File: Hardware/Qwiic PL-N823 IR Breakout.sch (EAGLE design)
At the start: 22 parts, among them U1 ADS1015, U2 LMV358, U3 PL-N823-01

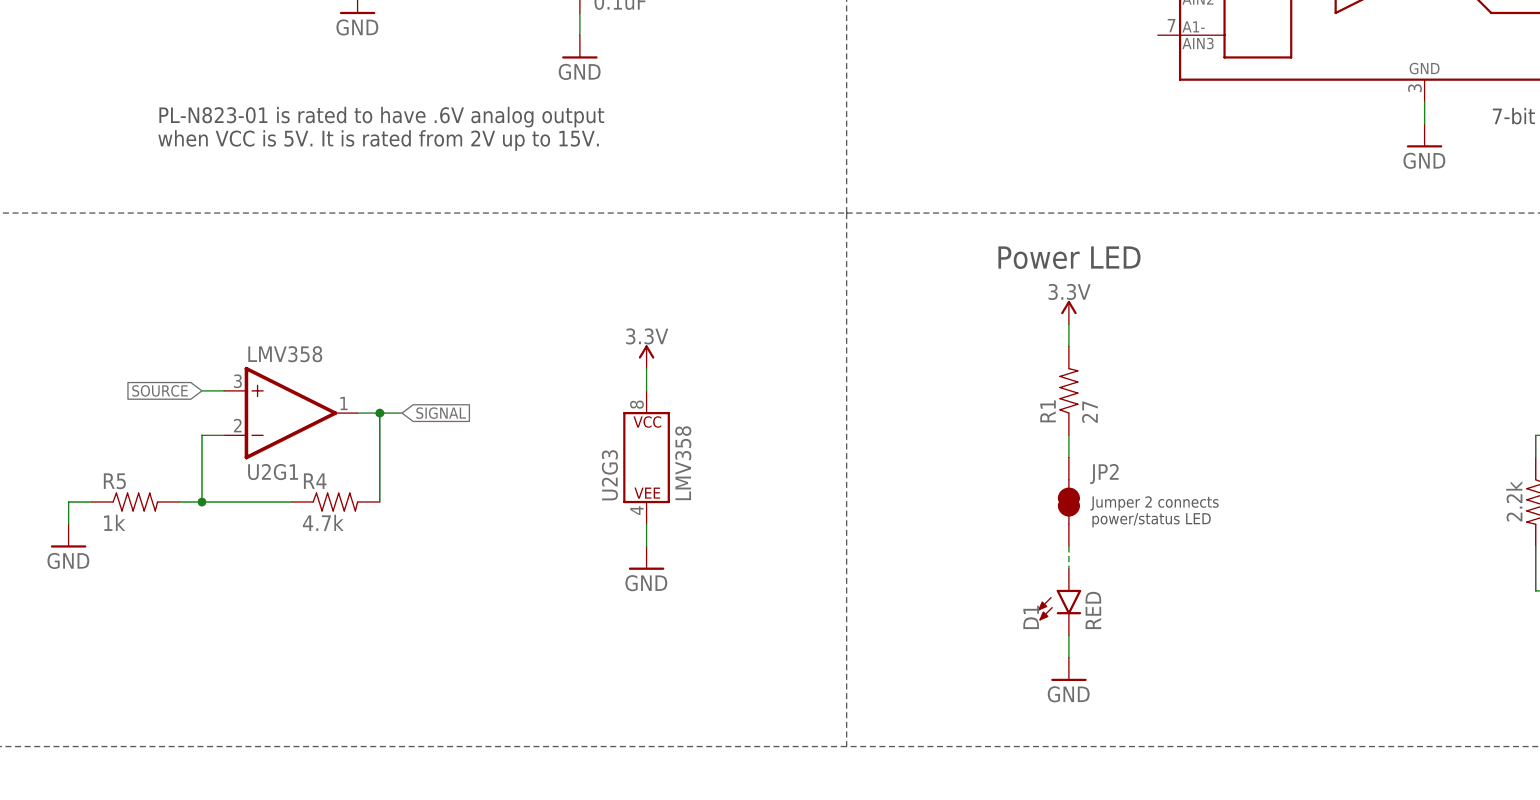
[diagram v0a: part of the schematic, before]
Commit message: Add no clean note. Change to blue power LED.
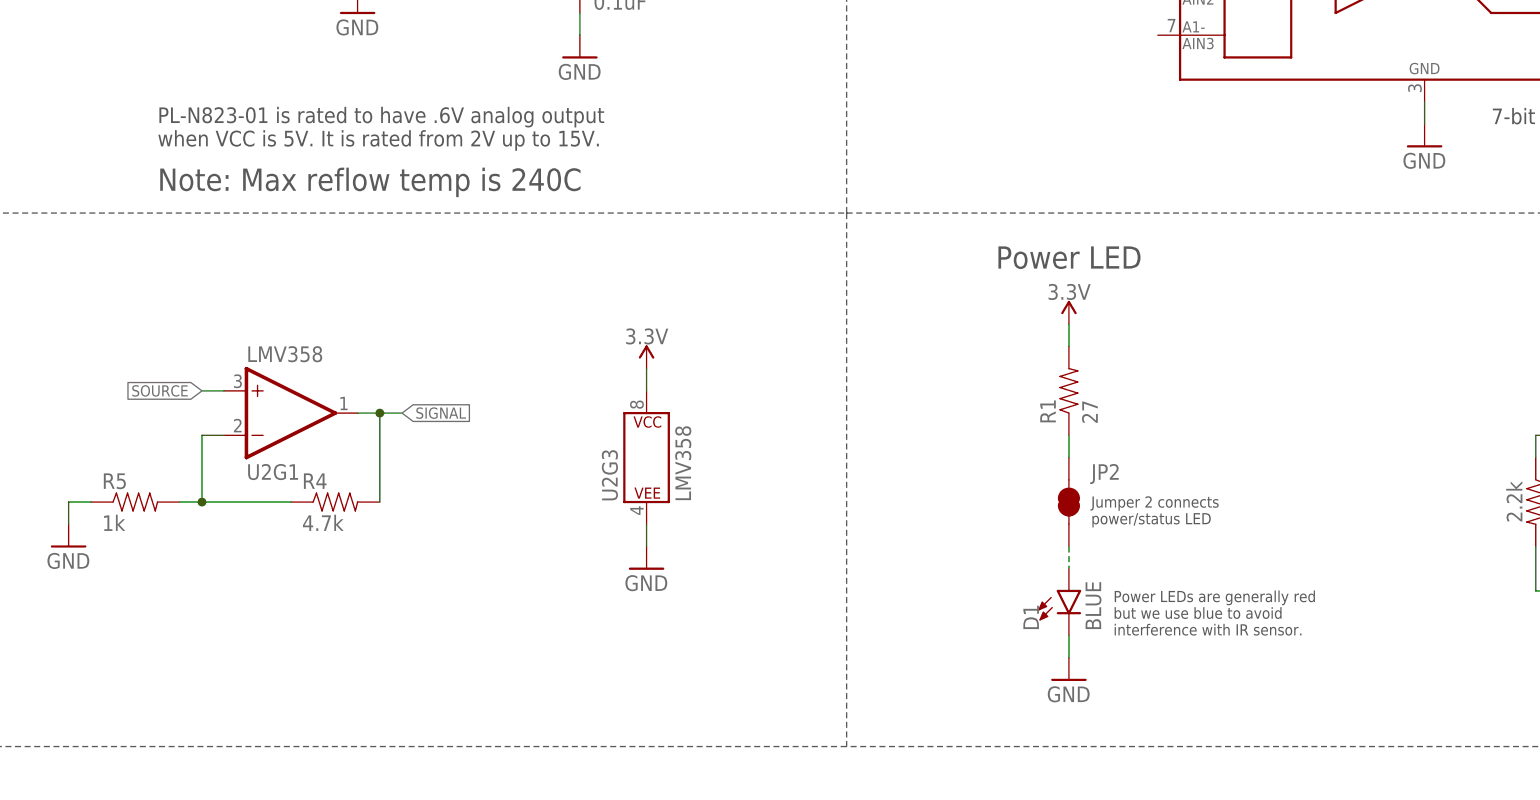
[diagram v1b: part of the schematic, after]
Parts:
- D1: value RED -> BLUE; device SparkFun-LED:LED-RED0603 -> SparkFun-LED:LED-BLUE0603
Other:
- note added: "Note: Max reflow temp is 240C"
- note added: "Power LEDs are generally red but we use blue to avoid interference with IR sensor."
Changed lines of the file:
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@@
 <part name="H1" library="SparkFun-Hardware" deviceset="STAND-OFF" device="TIGHT"/>
 <part name="H2" library="SparkFun-Hardware" deviceset="STAND-OFF" device="TIGHT"/>
-<part name="D1" library="SparkFun-LED" deviceset="LED-RED" device="0603" value="RED"/>
+<part name="D1" library="SparkFun-LED" deviceset="LED-BLUE" device="0603" value="BLUE"/>
 <part name="GND8" library="SparkFun-PowerSymbols" deviceset="GND" device=""/>
 <part name="GND9" library="SparkFun-PowerSymbols" deviceset="GND" device=""/>
@@
 <text x="101.6" y="48.26" size="2.54" layer="97" ratio="15" align="center">Connectors</text>
 <wire x1="111.76" y1="119.38" x2="248.92" y2="119.38" width="0.1524" layer="97" style="longdash"/>
+<text x="33.02" y="121.92" size="2.54" layer="97">Note: Max reflow temp is 240C</text>
+<text x="142.24" y="71.12" size="1.27" layer="97">Power LEDs are generally red
+but we use blue to avoid
+interference with IR sensor.</text>
 </plain>
 <instances>

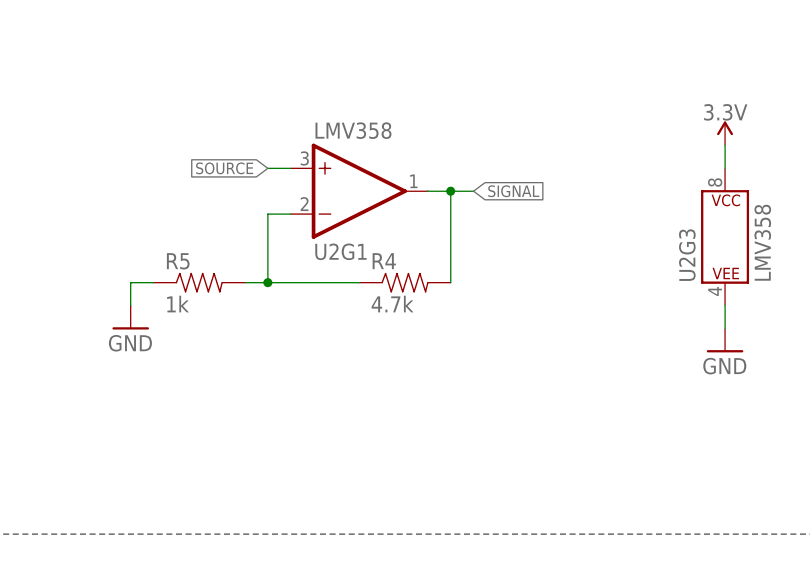
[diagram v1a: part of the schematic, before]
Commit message: Updated amplifier circuit
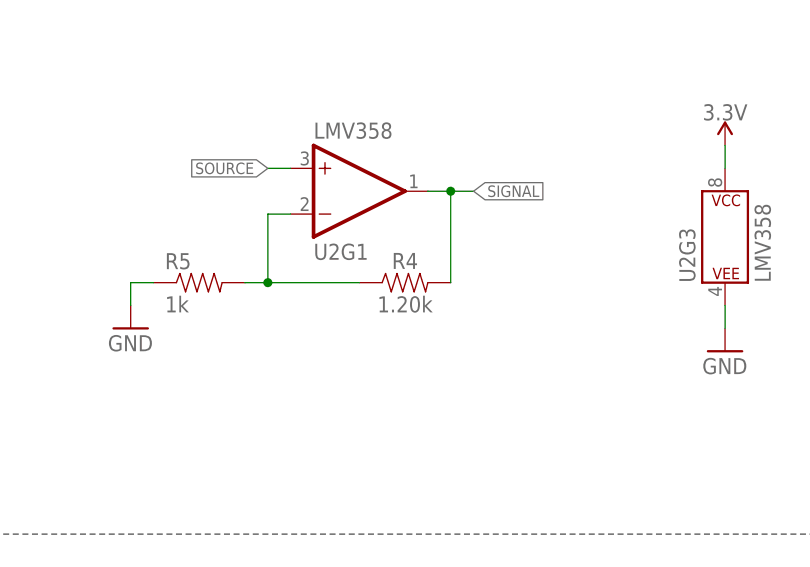
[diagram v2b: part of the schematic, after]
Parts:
- R4: value 4.7k -> 1.20k; device SparkFun-Resistors:4.7KOHM-0603-1/10W-1% -> SparkFun-Resistors:1.20KOHM-0603-1/10W-1%
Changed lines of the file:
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@@
 <?xml version="1.0" encoding="utf-8"?>
 <!DOCTYPE eagle SYSTEM "eagle.dtd">
-<eagle version="9.4.0">
+<eagle version="9.4.2">
 <drawing>
 <settings>
@@
 <part name="GND3" library="SparkFun-PowerSymbols" deviceset="GND" device=""/>
 <part name="GND4" library="SparkFun-PowerSymbols" deviceset="GND" device=""/>
-<part name="R4" library="SparkFun-Resistors" deviceset="4.7KOHM" device="-0603-1/10W-1%" value="4.7k"/>
 <part name="R5" library="SparkFun-Resistors" deviceset="1KOHM" device="-0603-1/10W-1%" value="1k"/>
 <part name="U2" library="SparkFun-IC-Amplifiers" deviceset="LMV358" device="SOIC" value="LMV358"/>
@@
 <part name="SUPPLY15" library="SparkFun-PowerSymbols" deviceset="3.3V" device=""/>
 <part name="SUPPLY16" library="SparkFun-PowerSymbols" deviceset="3.3V" device=""/>
+<part name="R4" library="SparkFun-Resistors" deviceset="1.20KOHM" device="-0603-1/10W-1%" value="1.20k"/>
 </parts>
 <sheets>
@@
 <attribute name="VALUE" x="20.32" y="78.74" size="1.778" layer="96"/>
 </instance>
-<instance part="R4" gate="G$1" x="53.34" y="86.36" smashed="yes">
-<attribute name="NAME" x="49.53" y="87.8586" size="1.778" layer="95"/>
-<attribute name="VALUE" x="49.53" y="83.058" size="1.778" layer="96"/>
-</instance>
 <instance part="R5" gate="G$1" x="30.48" y="86.36" smashed="yes">
 <attribute name="NAME" x="26.67" y="87.8586" size="1.778" layer="95"/>
@@
 <instance part="SUPPLY16" gate="G$1" x="198.12" y="101.6" smashed="yes">
 <attribute name="VALUE" x="198.12" y="104.394" size="1.778" layer="96" align="bottom-center"/>
+</instance>
+<instance part="R4" gate="G$1" x="53.34" y="86.36" smashed="yes">
+<attribute name="NAME" x="53.34" y="87.884" size="1.778" layer="95" font="vector" align="bottom-center"/>
+<attribute name="VALUE" x="53.34" y="84.836" size="1.778" layer="96" font="vector" align="top-center"/>
 </instance>
 </instances>
@@
 <wire x1="55.88" y1="96.52" x2="58.42" y2="96.52" width="0.1524" layer="91"/>
 <pinref part="U2" gate="G1" pin="OUT"/>
-<pinref part="R4" gate="G$1" pin="2"/>
 <wire x1="58.42" y1="96.52" x2="60.96" y2="96.52" width="0.1524" layer="91"/>
 <wire x1="58.42" y1="86.36" x2="58.42" y2="96.52" width="0.1524" layer="91"/>
 <junction x="58.42" y="96.52"/>
 <label x="60.96" y="96.52" size="1.27" layer="95" xref="yes"/>
+<pinref part="R4" gate="G$1" pin="2"/>
 </segment>
 <segment>
@@
 <pinref part="R5" gate="G$1" pin="2"/>
 <wire x1="38.1" y1="86.36" x2="35.56" y2="86.36" width="0.1524" layer="91"/>
-<pinref part="R4" gate="G$1" pin="1"/>
 <wire x1="38.1" y1="86.36" x2="48.26" y2="86.36" width="0.1524" layer="91"/>
 <junction x="38.1" y="86.36"/>
-</segment>
-</net>
+<pinref part="R4" gate="G$1" pin="1"/>
+</segment>
+</net>

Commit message: Transition to production: Added PROD_ID of IR sensor
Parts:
- U3: PROD_ID (none) -> IC-14725
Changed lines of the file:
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@@
 <part name="JP1" library="SparkFun-Jumpers" deviceset="JUMPER-SMT_3_2-NC_TRACE" device="_SILK" value="JUMPER-SMT_3_2-NC_TRACE_SILK"/>
 <part name="JP2" library="SparkFun-Jumpers" deviceset="JUMPER-SMT_2_NC_TRACE" device="_SILK" value="JUMPER-SMT_2_NC_TRACE_SILK"/>
-<part name="U3" library="PL-N823-01" deviceset="PL-N823-01" device=""/>
+<part name="U3" library="PL-N823-01" deviceset="PL-N823-01" device="">
+<attribute name="PROD_ID" value="IC-14725"/>
+</part>
 <part name="GND7" library="supply1" library_urn="urn:adsk.eagle:library:371" deviceset="GND" device=""/>
 <part name="H1" library="SparkFun-Hardware" deviceset="STAND-OFF" device="TIGHT"/>
@@
 <attribute name="NAME" x="30.48" y="165.1" size="1.778" layer="95"/>
 <attribute name="VALUE" x="30.48" y="152.4" size="1.778" layer="95"/>
+<attribute name="PROD_ID" x="38.1" y="160.02" size="1.27" layer="96" display="off"/>
 </instance>
 <instance part="GND7" gate="1" x="55.88" y="142.24" smashed="yes">
